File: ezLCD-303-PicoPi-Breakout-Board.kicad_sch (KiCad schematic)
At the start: 1 part

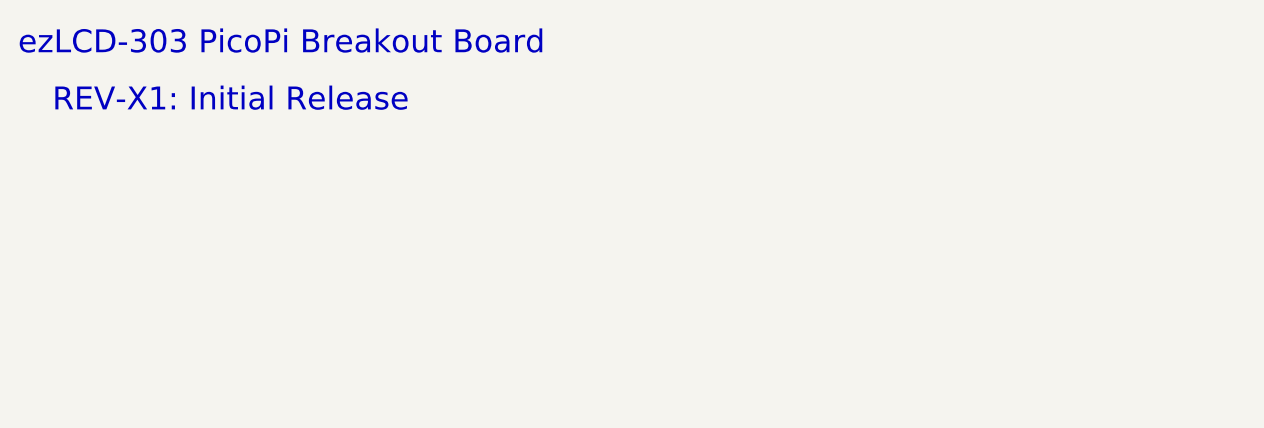
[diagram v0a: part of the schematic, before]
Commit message: Fixed errors on the schematic found after fabrication of the X1 PCB's.
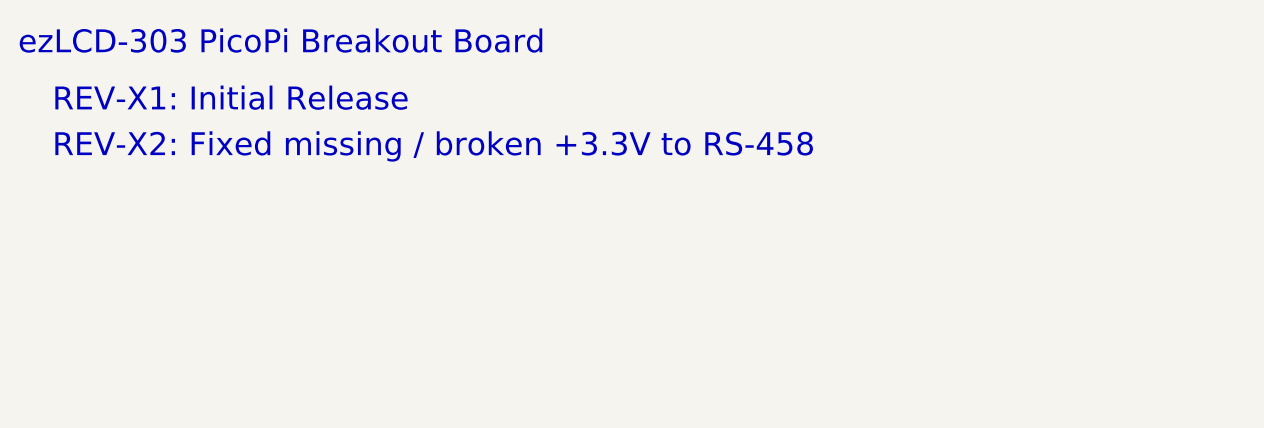
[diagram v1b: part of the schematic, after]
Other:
- note added: "REV-X2: Fixed missing / broken +3.3V to RS-458"
- company: (none) -> EarthLCD
- title: (none) -> ezLCDPK-3x
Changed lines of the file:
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@@
 (kicad_sch (version 20230121) (generator eeschema)
   (paper "A4")
+  (title_block
+    (title "ezLCDPK-3x")
+    (date "2023-10-27")
+    (rev "X2")
+    (company "EarthLCD")
+  )
   (bus (pts (xy 148.59 99.06) (xy 165.1 99.06))
     (stroke (width 0) (type default))
@@
     (effects (font (size 2.54 2.54)) (justify left bottom))
   )
+  (text "REV-X2: Fixed missing / broken +3.3V to RS-458" (at 20.32 31.75 0)
+    (effects (font (size 2.54 2.54)) (justify left bottom))
+  )
